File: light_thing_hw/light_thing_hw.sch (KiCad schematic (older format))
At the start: 55 parts, among them J1 CONNECTORS, J2 Li-Ion Battery, J3 ADDR_LED_PANEL_1_CONNECTORS, J4 ADDR_LED_PANEL_2_CONNECTORS, Q1 MMBF170, SW1 ST_USER_BUTTON1, SW2 ST_RESET_BUTTON, U1 BC832-V1, U2 LSM6DS3, U3 MCP73833T-FCI_UN, U4 LMR62421XMF, U5 LP38511MRX-ADJ_NOPB, U5A1 STM32L452RETx

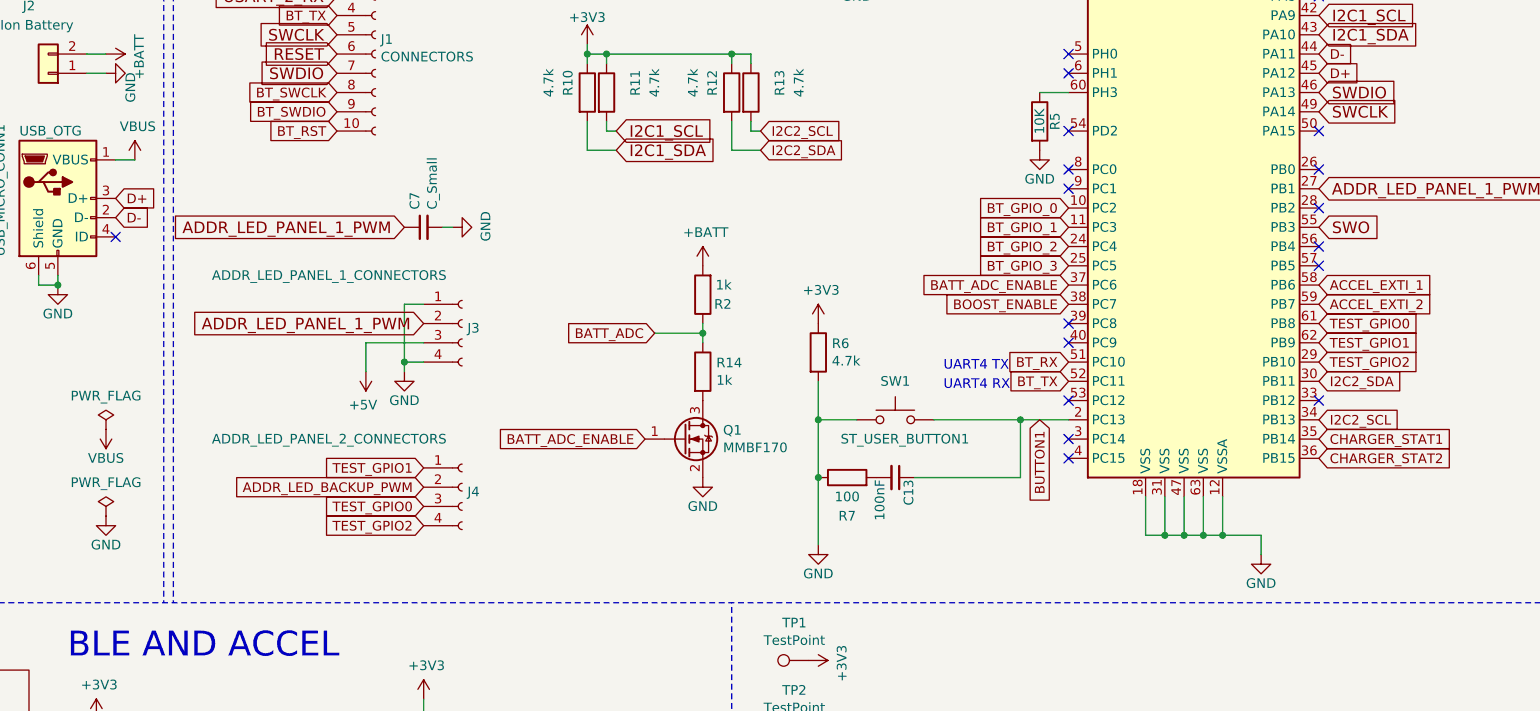
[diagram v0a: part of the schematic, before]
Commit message: added MIC_IN to hardware and in stmcube
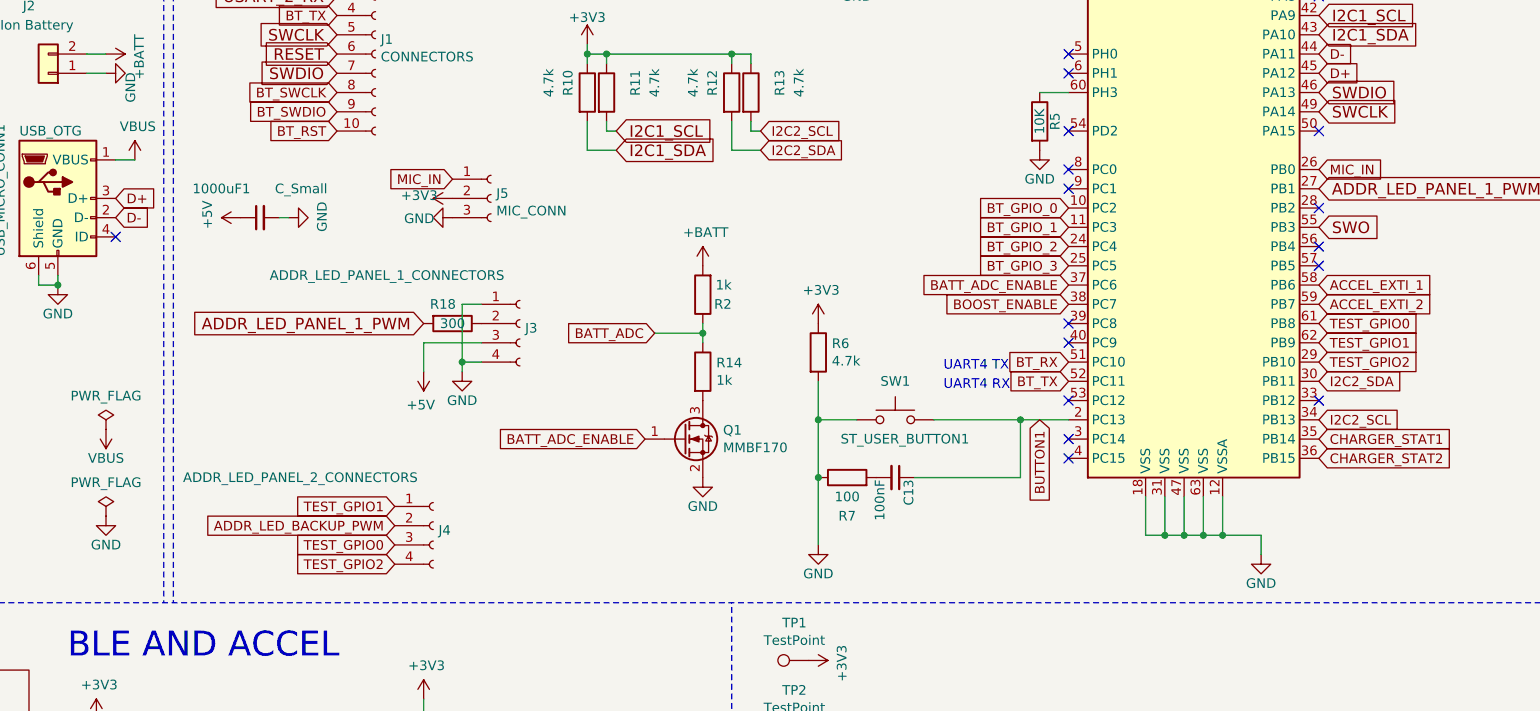
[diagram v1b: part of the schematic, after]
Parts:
- added J5: MIC_CONN, Connector_PinHeader_1.00mm:PinHeader_1x03_P1.00mm_Vertical, symbol Connector:Conn_01x03_Female
- added R18: 300, Resistor_SMD:R_0603_1608Metric_Pad1.05x0.95mm_HandSolder, symbol Device:R
- renumbered C7 to 1000uF1
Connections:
- net +3V3: now also J5.2 (Pin_2)
- net +5V: now also 1000uF1.1
- net ADDR_LED_PANEL_1_PWM: now also R18.2; no longer 1000uF1.1, J3.2 (Pin_2)
- net GND: now also J5.3 (Pin_3)
- net MIC_IN: now reaches U5A1.26 (PB0)
- net MIC_IN: now also J5.1 (Pin_1)
- new net: J3.2 (Pin_2), R18.1
- no-connect marks 46 -> 45
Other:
- moved on the sheet: 1000uF1, J3, J4
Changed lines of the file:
@@
 Text GLabel 3500 6000 2    50   Input ~ 0
 I2C2_SDA
-Text GLabel 5250 3250 0    60   Input ~ 0
-ADDR_LED_PANEL_1_PWM
-$Comp
-L Device:C_Small C7
+$Comp
+L Device:C_Small 1000uF1
 U 1 1 5ED59C90
-P 5350 3250
-F 0 "C7" H 5442 3296 50  0000 L CNN
-F 1 "C_Small" H 5442 3205 50  0000 L CNN
-F 2 "Capacitor_SMD:C_0603_1608Metric_Pad1.05x0.95mm_HandSolder" H 5350 3250 50  0001 C CNN
-F 3 "~" H 5350 3250 50  0001 C CNN
-	1    5350 3250
+P 4500 3200
+F 0 "1000uF1" V 4650 3250 50  0000 L CNN
+F 1 "C_Small" V 4650 2850 50  0000 L CNN
+F 2 "Capacitor_SMD:C_0603_1608Metric_Pad1.05x0.95mm_HandSolder" H 4500 3200 50  0001 C CNN
+F 3 "~" H 4500 3200 50  0001 C CNN
+	1    4500 3200
 	0    -1   -1   0
 $EndComp
@@
 L power:GND #PWR08
 U 1 1 5ED59DA5
-P 5500 3250
-F 0 "#PWR08" H 5500 3000 50  0001 C CNN
-F 1 "GND" H 5505 3077 50  0000 C CNN
-F 2 "" H 5500 3250 50  0001 C CNN
-F 3 "" H 5500 3250 50  0001 C CNN
-	1    5500 3250
+P 4650 3200
+F 0 "#PWR08" H 4650 2950 50  0001 C CNN
+F 1 "GND" H 4655 3027 50  0000 C CNN
+F 2 "" H 4650 3200 50  0001 C CNN
+F 3 "" H 4650 3200 50  0001 C CNN
+	1    4650 3200
 	0    -1   -1   0
 $EndComp
 Wire Wire Line
-	5500 3250 5450 3250
+	4650 3200 4600 3200
 $Comp
 L power:GND #PWR016
@@
 L Connector:Conn_01x04_Female J3
 U 1 1 5F21F6BE
-P 5550 3750
-F 0 "J3" H 5577 3726 50  0000 L CNN
-F 1 "ADDR_LED_PANEL_1_CONNECTORS" H 4250 4000 50  0000 L CNN
-F 2 "Connector_PinHeader_1.00mm:PinHeader_2x02_P1.00mm_Vertical" H 5550 3750 50  0001 C CNN
-F 3 "~" H 5550 3750 50  0001 C CNN
-	1    5550 3750
+P 5850 3750
+F 0 "J3" H 5877 3726 50  0000 L CNN
+F 1 "ADDR_LED_PANEL_1_CONNECTORS" H 4550 4000 50  0000 L CNN
+F 2 "Connector_PinHeader_1.00mm:PinHeader_2x02_P1.00mm_Vertical" H 5850 3750 50  0001 C CNN
+F 3 "~" H 5850 3750 50  0001 C CNN
+	1    5850 3750
 	1    0    0    -1
 $EndComp
@@
 L power:GND #PWR0110
 U 1 1 5F2443F1
-P 5250 4000
-F 0 "#PWR0110" H 5250 3750 50  0001 C CNN
-F 1 "GND" H 5250 3850 50  0000 C CNN
-F 2 "" H 5250 4000 50  0001 C CNN
-F 3 "" H 5250 4000 50  0001 C CNN
-	1    5250 4000
-	1    0    0    -1
-$EndComp
-Wire Wire Line
-	5350 3650 5250 3650
-Wire Wire Line
-	5250 3650 5250 3950
-Wire Wire Line
-	5350 3950 5250 3950
-Connection ~ 5250 3950
-Wire Wire Line
-	5250 3950 5250 4000
+P 5550 4000
+F 0 "#PWR0110" H 5550 3750 50  0001 C CNN
+F 1 "GND" H 5550 3850 50  0000 C CNN
+F 2 "" H 5550 4000 50  0001 C CNN
+F 3 "" H 5550 4000 50  0001 C CNN
+	1    5550 4000
+	1    0    0    -1
+$EndComp
+Wire Wire Line
+	5650 3650 5550 3650
+Wire Wire Line
+	5550 3650 5550 3950
+Wire Wire Line
+	5650 3950 5550 3950
+Connection ~ 5550 3950
+Wire Wire Line
+	5550 3950 5550 4000
 $Comp
 L power:+5V #PWR0111
 U 1 1 5F257396
-P 5050 4000
-F 0 "#PWR0111" H 5050 3850 50  0001 C CNN
-F 1 "+5V" H 5065 4173 50  0000 C CNN
-F 2 "" H 5050 4000 50  0001 C CNN
-F 3 "" H 5050 4000 50  0001 C CNN
-	1    5050 4000
+P 5350 4000
+F 0 "#PWR0111" H 5350 3850 50  0001 C CNN
+F 1 "+5V" H 5365 4173 50  0000 C CNN
+F 2 "" H 5350 4000 50  0001 C CNN
+F 3 "" H 5350 4000 50  0001 C CNN
+	1    5350 4000
 	-1   0    0    1
 $EndComp
 Wire Wire Line
-	5350 3850 5050 3850
-Wire Wire Line
-	5050 3850 5050 4000
+	5650 3850 5350 3850
+Wire Wire Line
+	5350 3850 5350 4000
 $Comp
 L Connector:Conn_01x04_Female J4
 U 1 1 5F270378
-P 5550 4600
-F 0 "J4" H 5577 4576 50  0000 L CNN
-F 1 "ADDR_LED_PANEL_2_CONNECTORS" H 4250 4850 50  0000 L CNN
-F 2 "Connector_PinHeader_1.00mm:PinHeader_2x02_P1.00mm_Vertical" H 5550 4600 50  0001 C CNN
-F 3 "~" H 5550 4600 50  0001 C CNN
-	1    5550 4600
+P 5400 4800
+F 0 "J4" H 5427 4776 50  0000 L CNN
+F 1 "ADDR_LED_PANEL_2_CONNECTORS" H 4100 5050 50  0000 L CNN
+F 2 "Connector_PinHeader_1.00mm:PinHeader_2x02_P1.00mm_Vertical" H 5400 4800 50  0001 C CNN
+F 3 "~" H 5400 4800 50  0001 C CNN
+	1    5400 4800
 	1    0    0    -1
 $EndComp
@@
 NoConn ~ 10000 2050
 NoConn ~ 10000 2750
-NoConn ~ 10000 2950
 NoConn ~ 10000 3150
 NoConn ~ 10000 3350
@@
 Text GLabel 10000 3950 2    50   Input ~ 0
 TEST_GPIO2
-Text GLabel 5350 4600 0    50   Input ~ 0
+Text GLabel 5200 4800 0    50   Input ~ 0
 ADDR_LED_BACKUP_PWM
 NoConn ~ 10000 4150
-Text GLabel 5350 4700 0    50   Input ~ 0
+Text GLabel 5200 4900 0    50   Input ~ 0
 TEST_GPIO0
-Text GLabel 5350 4500 0    50   Input ~ 0
+Text GLabel 5200 4700 0    50   Input ~ 0
 TEST_GPIO1
-Text GLabel 5350 4800 0    50   Input ~ 0
+Text GLabel 5200 5000 0    50   Input ~ 0
 TEST_GPIO2
 $Comp
@@
 	0    -1   -1   0
 $EndComp
+$Comp
+L power:+5V #PWR0113
+U 1 1 5F0C7F22
+P 4400 3200
+F 0 "#PWR0113" H 4400 3050 50  0001 C CNN
+F 1 "+5V" H 4415 3373 50  0000 C CNN
+F 2 "" H 4400 3200 50  0001 C CNN
+F 3 "" H 4400 3200 50  0001 C CNN
+	1    4400 3200
+	0    -1   -1   0
+$EndComp
+$Comp
+L Device:R R18
+U 1 1 5F104033
+P 5500 3750
+F 0 "R18" V 5400 3700 50  0000 C CNN
+F 1 "300" V 5500 3750 50  0000 C CNN
+F 2 "Resistor_SMD:R_0603_1608Metric_Pad1.05x0.95mm_HandSolder" V 5430 3750 50  0001 C CNN
+F 3 "~" H 5500 3750 50  0001 C CNN
+	1    5500 3750
+	0    1    1    0
+$EndComp
+$Comp
+L Connector:Conn_01x03_Female J5
+U 1 1 5F0C4A90
+P 5700 3100
+F 0 "J5" H 5727 3126 50  0000 L CNN
+F 1 "MIC_CONN" H 5727 3035 50  0000 L CNN
+F 2 "Connector_PinHeader_1.00mm:PinHeader_1x03_P1.00mm_Vertical" H 5700 3100 50  0001 C CNN
+F 3 "~" H 5700 3100 50  0001 C CNN
+	1    5700 3100
+	1    0    0    -1
+$EndComp
+$Comp
+L power:+3V3 #PWR013
+U 1 1 5F0DFE7A
+P 5500 3100
+F 0 "#PWR013" H 5500 2950 50  0001 C CNN
+F 1 "+3V3" V 5515 3273 50  0000 C CNN
+F 2 "" H 5500 3100 50  0001 C CNN
+F 3 "" H 5500 3100 50  0001 C CNN
+	1    5500 3100
+	0    -1   -1   0
+$EndComp
+$Comp
+L power:GND #PWR014
+U 1 1 5F0DFE80
+P 5500 3200
+F 0 "#PWR014" H 5500 2950 50  0001 C CNN
+F 1 "GND" V 5505 3027 50  0000 C CNN
+F 2 "" H 5500 3200 50  0001 C CNN
+F 3 "" H 5500 3200 50  0001 C CNN
+	1    5500 3200
+	0    1    1    0
+$EndComp
+Text GLabel 10000 2950 2    50   Input ~ 0
+MIC_IN
+Text GLabel 5500 3000 0    50   Input ~ 0
+MIC_IN
 $EndSCHEMATC

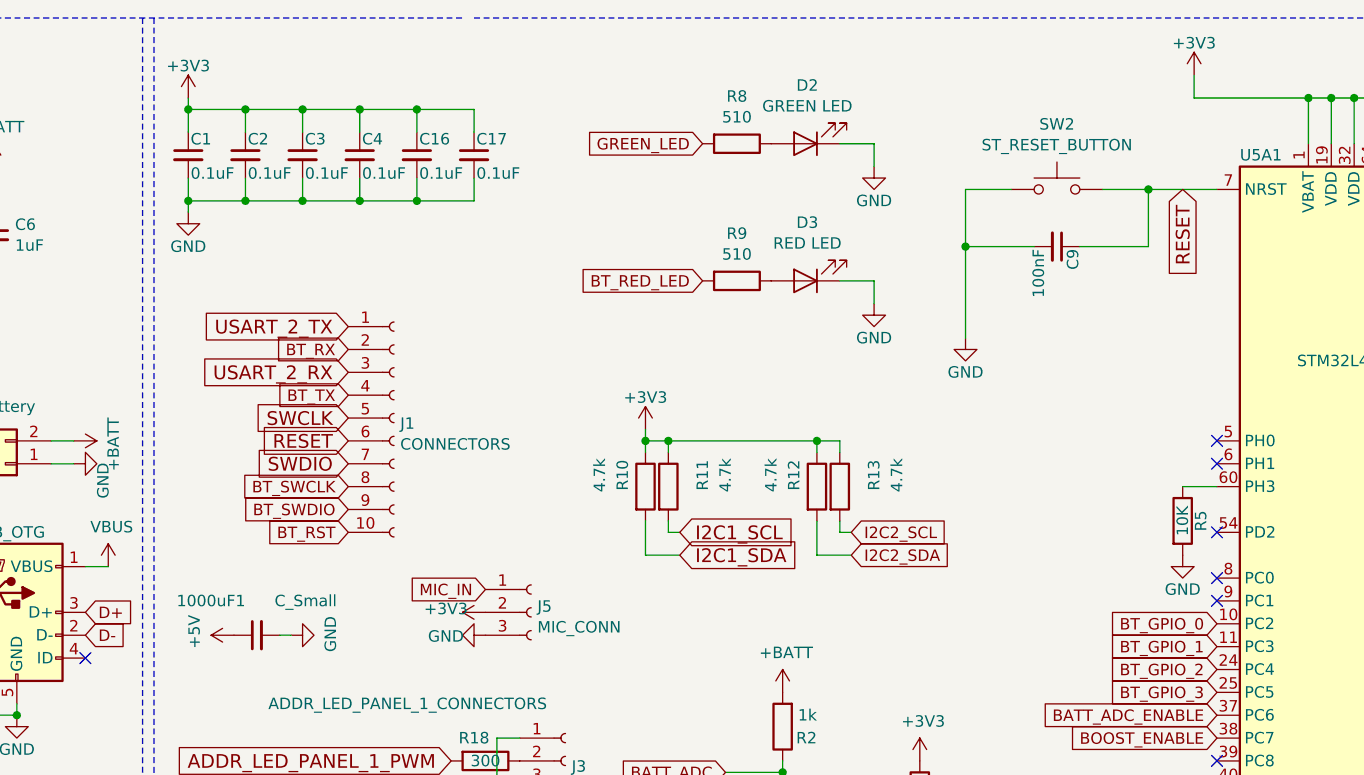
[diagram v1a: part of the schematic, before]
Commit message: some sw changes. about to add another mosfet switch to the board for the mic
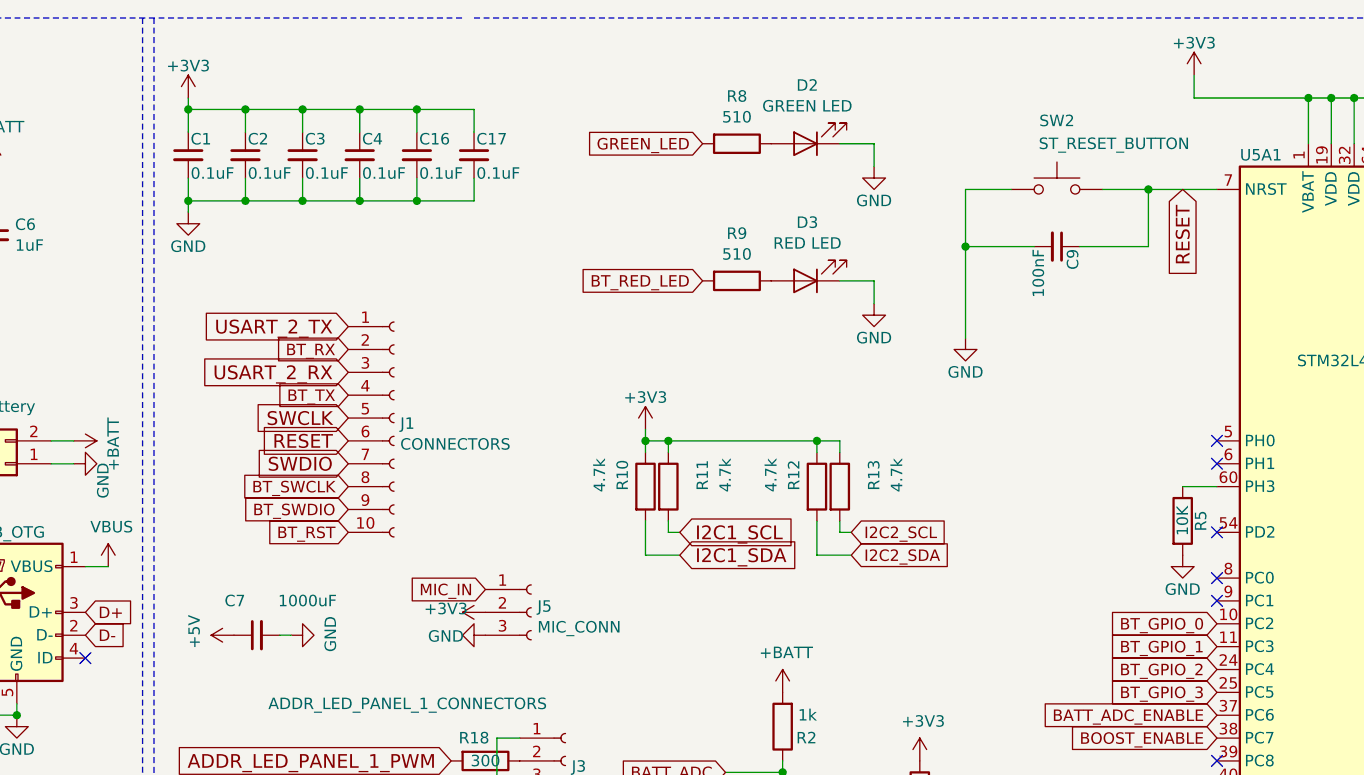
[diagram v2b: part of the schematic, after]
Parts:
- C7: renamed from 1000uF1; value C_Small -> 1000uF
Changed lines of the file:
@@
 I2C2_SDA
 $Comp
-L Device:C_Small 1000uF1
+L Device:C_Small C7
 U 1 1 5ED59C90
 P 4500 3200
-F 0 "1000uF1" V 4650 3250 50  0000 L CNN
-F 1 "C_Small" V 4650 2850 50  0000 L CNN
+F 0 "C7" V 4650 3250 50  0000 L CNN
+F 1 "1000uF" V 4650 2850 50  0000 L CNN
 F 2 "Capacitor_SMD:C_0603_1608Metric_Pad1.05x0.95mm_HandSolder" H 4500 3200 50  0001 C CNN
 F 3 "~" H 4500 3200 50  0001 C CNN
@@
 U 1 1 5F1F7301
 P 8000 1250
-F 0 "SW2" H 8000 1535 50  0000 C CNN
-F 1 "ST_RESET_BUTTON" H 8000 1444 50  0000 C CNN
+F 0 "SW2" H 8000 1550 50  0000 C CNN
+F 1 "ST_RESET_BUTTON" H 8250 1450 50  0000 C CNN
 F 2 "Button_Switch_SMD:SW_SPST_CK_RS282G05A3" H 8000 1450 50  0001 C CNN
 F 3 "" H 8000 1450 50  0001 C CNN
